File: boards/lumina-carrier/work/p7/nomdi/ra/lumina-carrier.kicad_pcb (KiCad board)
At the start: 4 copper layers, 100 x 80 mm, 116 parts, among them J1 LPJG0926HENL PoE+ RJ45 magjack, J2 1x6 2.54mm header (recovery), J3 DS1021-2x7SF11-B 2x7 male hea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, J4 DS1021-2x12SF11-B 2x12 male h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, SW1 SMD tactile switch, U1 TPS2378DDAR, U10 W5500, U20 SCT2A25STER, U21 TPS563201DDCR, U22 TPS16630PWPR, U30 ESP32-S3-WROOM-1-N8, Y10 25MHz 18pF CL crystal

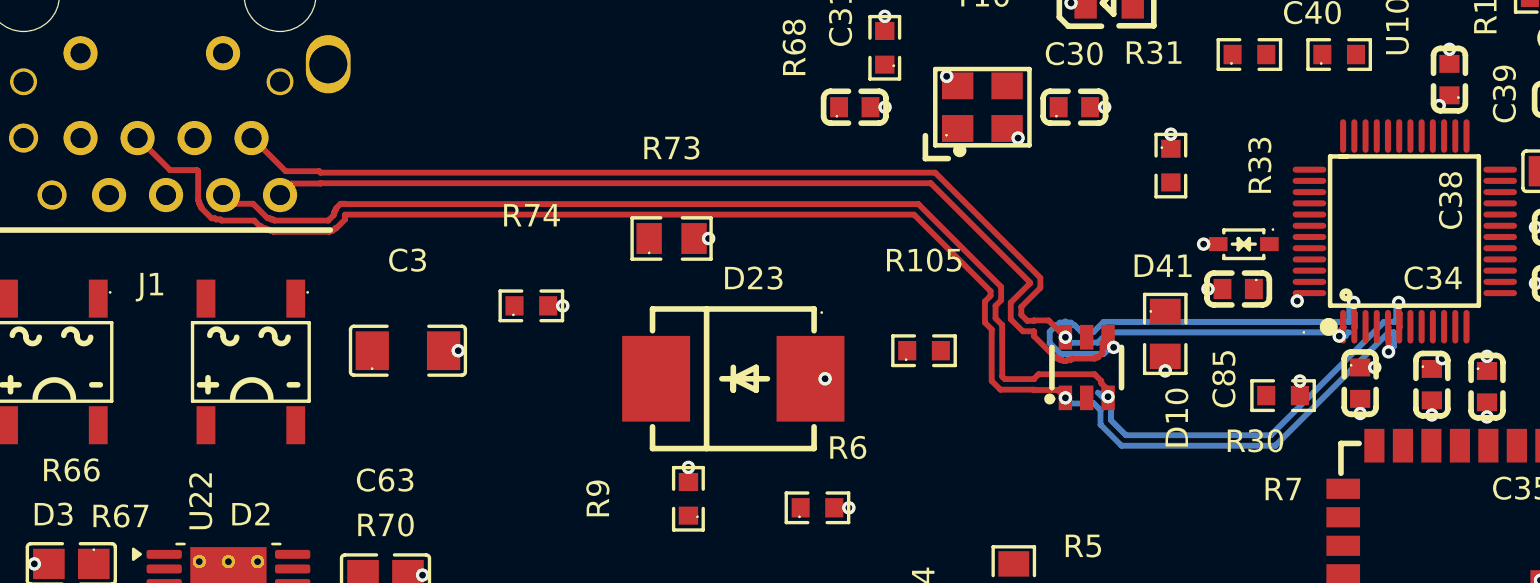
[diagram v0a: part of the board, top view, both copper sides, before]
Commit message: ai-ee lumina-carrier: P7 partial - planes, rule areas, MDI pairs, thermal stitching (177 unrouted)
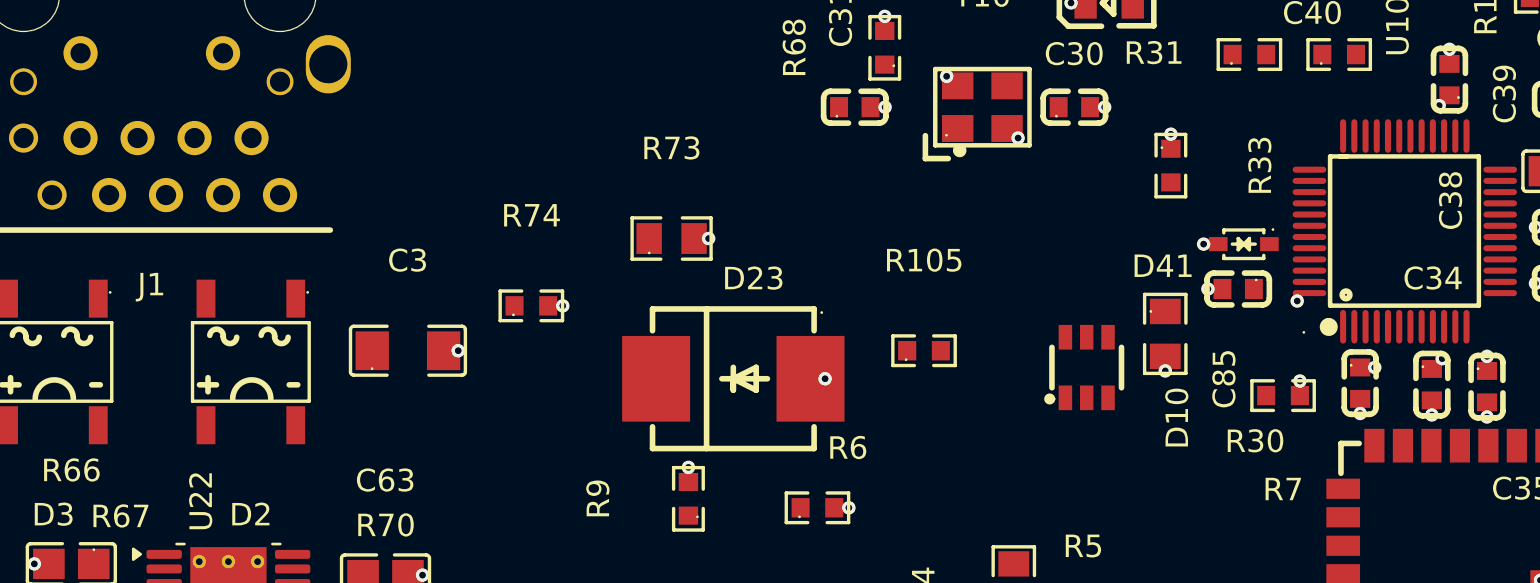
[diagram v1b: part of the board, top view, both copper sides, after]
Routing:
- net /ETH_RXN: track 70.4 -> 0.00 mm, vias 2 -> 0
- net /ETH_RXP: track 65.7 -> 0.00 mm, vias 2 -> 0
- net /ETH_TXP: track 63.7 -> 0.00 mm, vias 2 -> 0
- net /ETH_TXN: track 55.9 -> 0.00 mm, vias 2 -> 0
